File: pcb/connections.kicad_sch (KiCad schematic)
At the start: 5 parts, among them J201 Conn_01x20_Female, J202 Conn_01x20_Female, J203 Conn_01x20_Female, J204 Conn_01x20_Female, J205 Conn_01x20_Female

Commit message: schematic reworked, it's time to relayout the board. checkpoint here
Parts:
- removed J204, J205: Conn_01x20_Female, Connector_PinSocket_2.54mm:PinSocket_1x20_P2.54mm_Vertical, symbol Connector:Conn_01x20_Female
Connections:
- net P2_GPIO16: now also J202.7 (Pin_7)
- net P2_GPIO17: now also J202.8 (Pin_8)
- net P2_GPIO18: now also J202.9 (Pin_9)
- net P2_GPIO26: now also J202.15 (Pin_15)
- net P2_GPIO27: now also J202.16 (Pin_16)
- net P2_GPIO28: now also J202.17 (Pin_17)
- net ZX12V: now also J202.20 (Pin_20); no longer J201.20 (Pin_20)
- net ZX12VAC: no longer J202.5 (Pin_5)
- net ZX9V: now also J202.18 (Pin_18); no longer J203.4 (Pin_4)
- net ZXA0: now also J203.5 (Pin_5); no longer J203.6 (Pin_6)
- net ZXA1: now also J203.6 (Pin_6); no longer J203.7 (Pin_7)
- net ZXA10: now also J202.2 (Pin_2); no longer J202.9 (Pin_9)
- net ZXA11: now also J202.3 (Pin_3); no longer J202.4 (Pin_4)
- net ZXA2: now also J203.7 (Pin_7); no longer J203.8 (Pin_8)
- net ZXA3: now also J203.8 (Pin_8); no longer J203.9 (Pin_9)
- net ZXA4: now also J203.19 (Pin_19); no longer J203.20 (Pin_20)
- net ZXA5: now also J203.18 (Pin_18); no longer J203.19 (Pin_19)
- net ZXA6: now also J203.17 (Pin_17); no longer J203.18 (Pin_18)
- net ZXA7: now also J203.16 (Pin_16); no longer J203.17 (Pin_17)
- net ZXA8: now also J202.1 (Pin_1); no longer J202.8 (Pin_8)
- net ZXA9: now also J202.4 (Pin_4); no longer J202.3 (Pin_3)
- net ZXBUSACK: now also J202.5 (Pin_5); no longer J202.2 (Pin_2)
- net ZXBUSRQ: now also J203.14 (Pin_14); no longer J203.15 (Pin_15)
- net ZXCLK: now also J203.4 (Pin_4); no longer J203.5 (Pin_5)
- net ZXIORQGE: now also J203.9 (Pin_9); no longer J203.10 (Pin_10)
- net ZXM1: now also J201.19 (Pin_19); no longer J202.6 (Pin_6)
- net ZXMIN5V: now also J202.19 (Pin_19); no longer J201.18 (Pin_18)
- net ZXRESET: now also J203.15 (Pin_15); no longer J203.16 (Pin_16)
- net ZXRFSH: now also J201.20 (Pin_20); no longer J202.7 (Pin_7)
- net ZXROMCS: now also J203.20 (Pin_20); no longer J202.1 (Pin_1)
- net ZXU: now also J203.13 (Pin_13); no longer J203.14 (Pin_14)
- net ZXV: now also J203.12 (Pin_12); no longer J203.13 (Pin_13)
- net ZXVIDEO: now also J203.10 (Pin_10); no longer J203.11 (Pin_11)
- net ZXWAIT: now also J201.18 (Pin_18); no longer J201.19 (Pin_19)
- net ZXY: now also J203.11 (Pin_11); no longer J203.12 (Pin_12)
- net P1_BLIPPER: now reaches J202.13 (Pin_13)
- net P2_BLIPPER: now reaches J202.14 (Pin_14)
- new net PICO_SIGNAL: J202.6 (Pin_6)
- no-connect marks 8 -> 1
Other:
- note added: "I'm one short on these 3 connectors. This is the one I chose to sacrifice."
- note added: "These 3 are the dangerous ones. Accidentally connecting one of these to a Pico GPIO would fry the Pico, so they are isolated at this end of the connector"

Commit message: v1.1 off for fabrication
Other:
- title: (none) -> ZX Spectrum Diagnostics
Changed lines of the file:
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@@
   (paper "A4")
   (title_block
-    (date "2023-11-02")
+    (title "ZX Spectrum Diagnostics")
+    (date "2023-11-30")
+    (rev "1.1")
   )
   (no_connect (at 91.694 113.03))

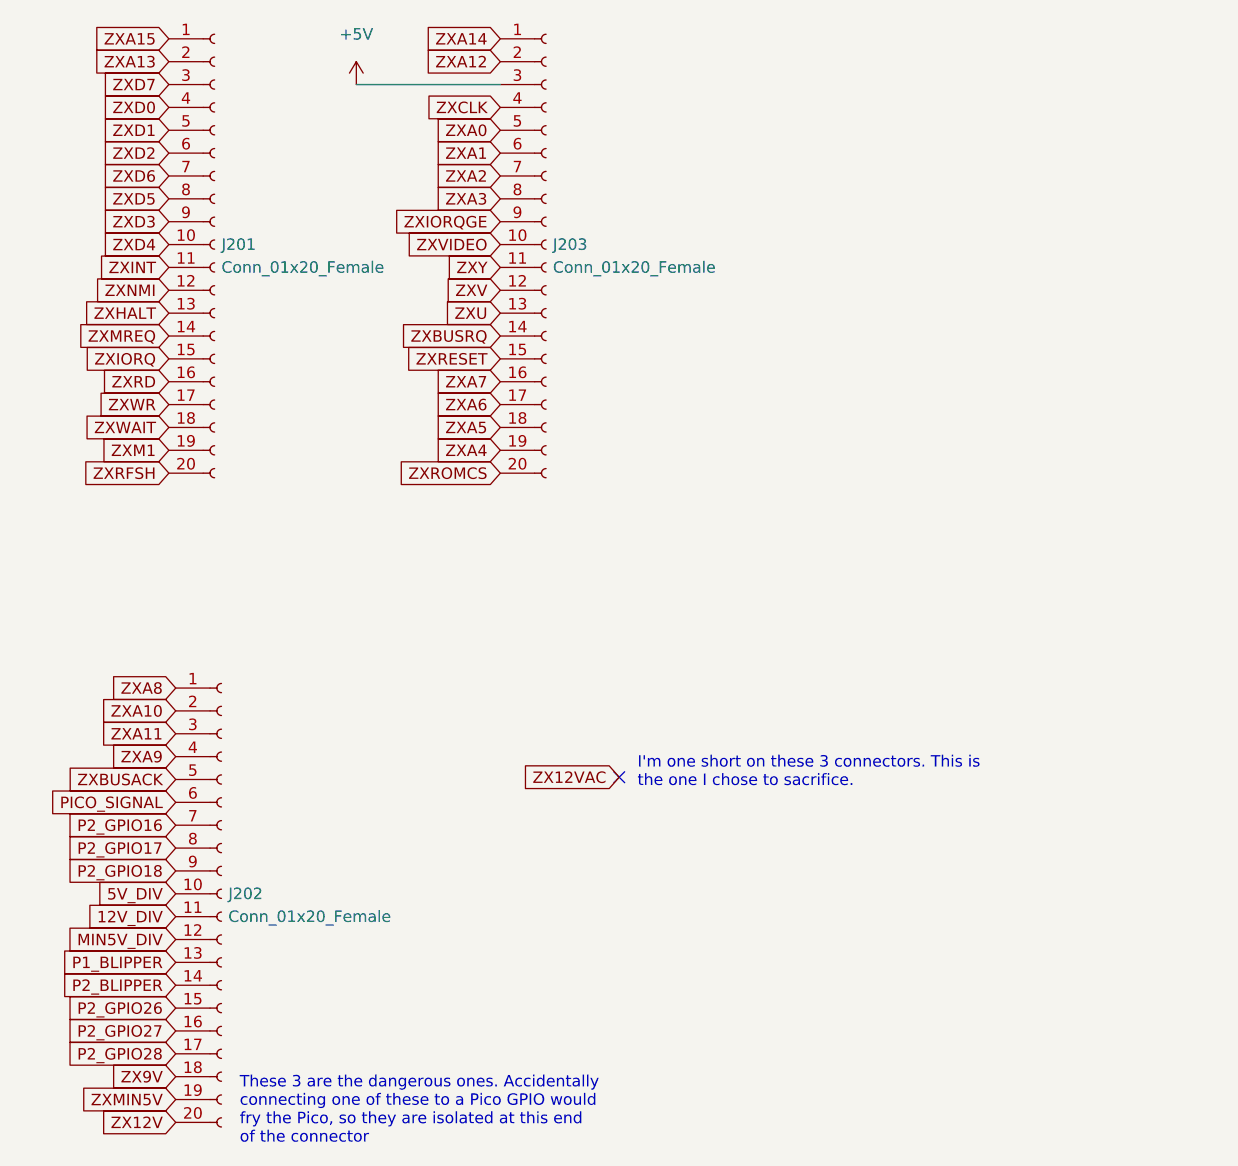
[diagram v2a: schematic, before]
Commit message: have a required test value sent over to pico2 at the start. add test code to fill the address buffer. works but shows the odd restarting effect i saw when i was doing the ROM emulator
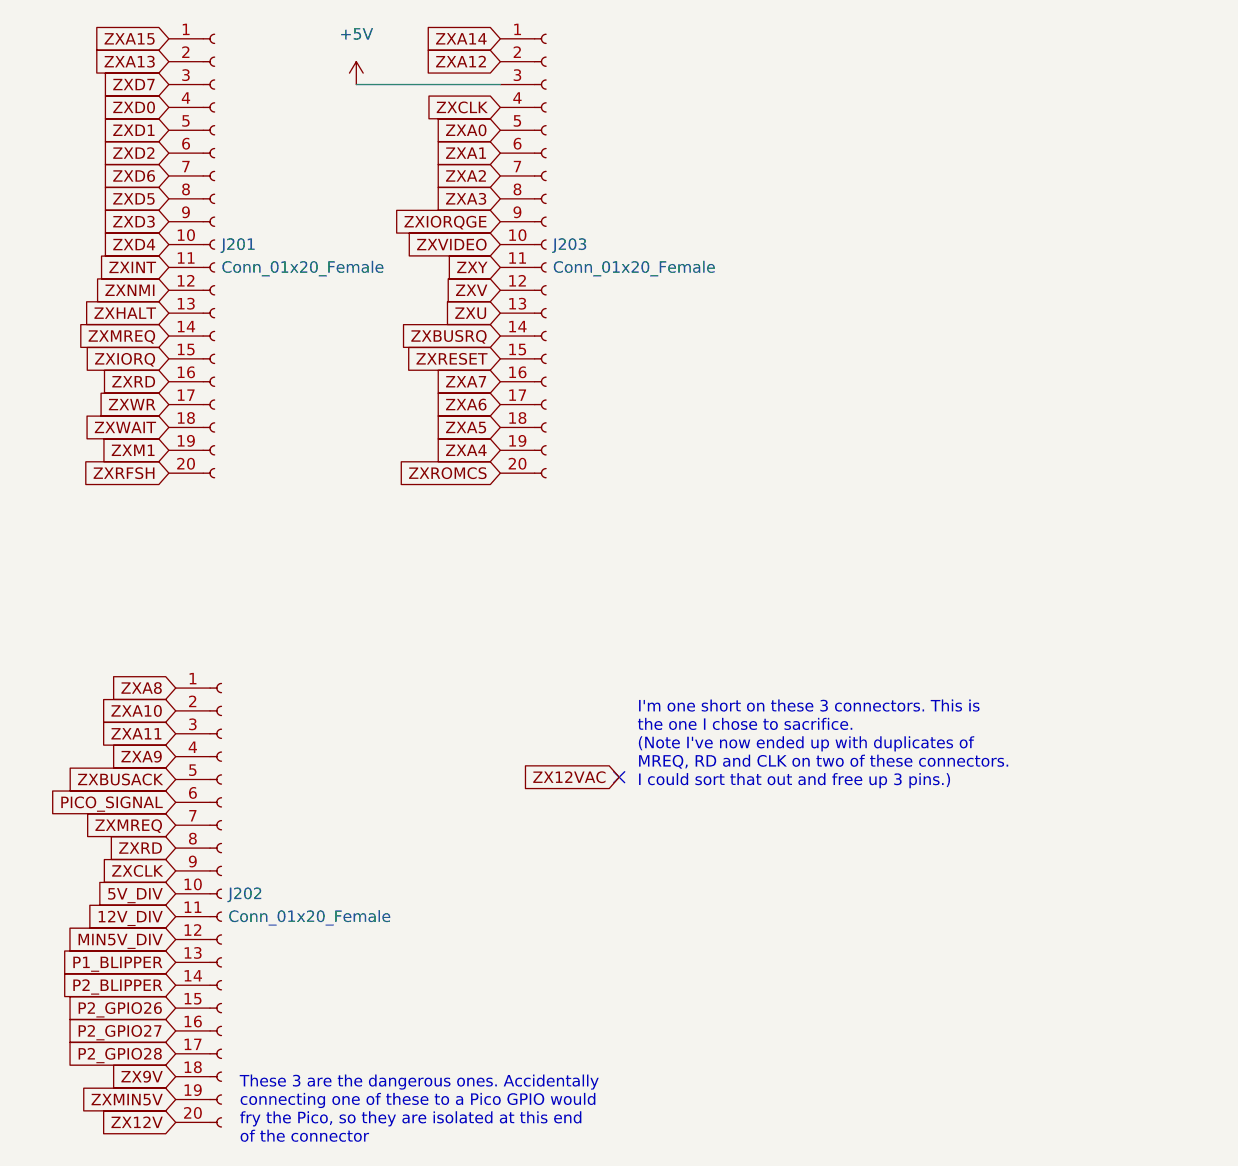
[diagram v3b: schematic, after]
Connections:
- net P2_GPIO16 is gone; now on net ZXMREQ: J202.7 (Pin_7)
- net P2_GPIO17 is gone; now on net ZXRD: J202.8 (Pin_8)
- net P2_GPIO18 is gone; now on net ZXCLK: J202.9 (Pin_9)
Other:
- note added: "I'm one short on these 3 connectors. This is the one I chose to sacrifice. (Note I've now ended up with duplicates of MREQ, RD and CLK on two of these connectors. I could sort that out and free up 3 pins.)"
- note removed: "I'm one short on these 3 connectors. This is the one I chose to sacrifice."
- title: ZX Spectrum Diagnostics -> ZX Spectrum Diagnostics Board
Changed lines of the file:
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@@
   (paper "A4")
   (title_block
-    (title "ZX Spectrum Diagnostics")
-    (date "2023-11-30")
-    (rev "1.1")
+    (title "ZX Spectrum Diagnostics Board")
+    (date "2024-02-22")
+    (rev "v1.2")
   )
   (no_connect (at 91.694 113.03))
@@
     (effects (font (size 1.27 1.27)) (justify left bottom))
   )
-  (text "I'm one short on these 3 connectors. This is\nthe one I chose to sacrifice."
+  (text "I'm one short on these 3 connectors. This is\nthe one I chose to sacrifice.\n(Note I've now ended up with duplicates of\nMREQ, RD and CLK on two of these connectors.\nI could sort that out and free up 3 pins.)"
     (at 93.726 114.3 0)
     (effects (font (size 1.27 1.27)) (justify left bottom))
@@
     )
   )
-  (global_label "P2_GPIO17" (shape input) (at 42.418 120.904 180) (fields_autoplaced)
-    (effects (font (size 1.27 1.27)) (justify right))
-    (property "Intersheet References" "${INTERSHEET_REFS}" (id 0) (at 29.6635 120.8246 0)
+  (global_label "ZXRD" (shape input) (at 42.418 120.904 180) (fields_autoplaced)
+    (effects (font (size 1.27 1.27)) (justify right))
+    (property "Intersheet References" "${INTERSHEET_REFS}" (id 0) (at 35.0459 120.8246 0)
       (effects (font (size 1.27 1.27)) (justify right) hide)
     )
@@
     )
   )
-  (global_label "P2_GPIO16" (shape input) (at 42.418 118.364 180) (fields_autoplaced)
-    (effects (font (size 1.27 1.27)) (justify right))
-    (property "Intersheet References" "${INTERSHEET_REFS}" (id 0) (at 29.6635 118.2846 0)
+  (global_label "ZXMREQ" (shape input) (at 42.418 118.364 180) (fields_autoplaced)
+    (effects (font (size 1.27 1.27)) (justify right))
+    (property "Intersheet References" "${INTERSHEET_REFS}" (id 0) (at 32.3849 118.2846 0)
       (effects (font (size 1.27 1.27)) (justify right) hide)
     )
@@
     )
   )
-  (global_label "P2_GPIO18" (shape input) (at 42.418 123.444 180) (fields_autoplaced)
-    (effects (font (size 1.27 1.27)) (justify right))
-    (property "Intersheet References" "${INTERSHEET_REFS}" (id 0) (at 29.6635 123.3646 0)
-      (effects (font (size 1.27 1.27)) (justify right) hide)
-    )
+  (global_label "ZXCLK" (shape input) (at 42.418 123.444 180) (fields_autoplaced)
+    (effects (font (size 1.27 1.27)) (justify right))
+    (property "Intersheet References" "${INTERSHEET_REFS}" (id 0) (at 34.0178 123.3646 0)
+      (effects (font (size 1.27 1.27)) (justify right) hide)
+    )
